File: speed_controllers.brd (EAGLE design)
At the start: 147.3 x 147.3 mm, 18 parts

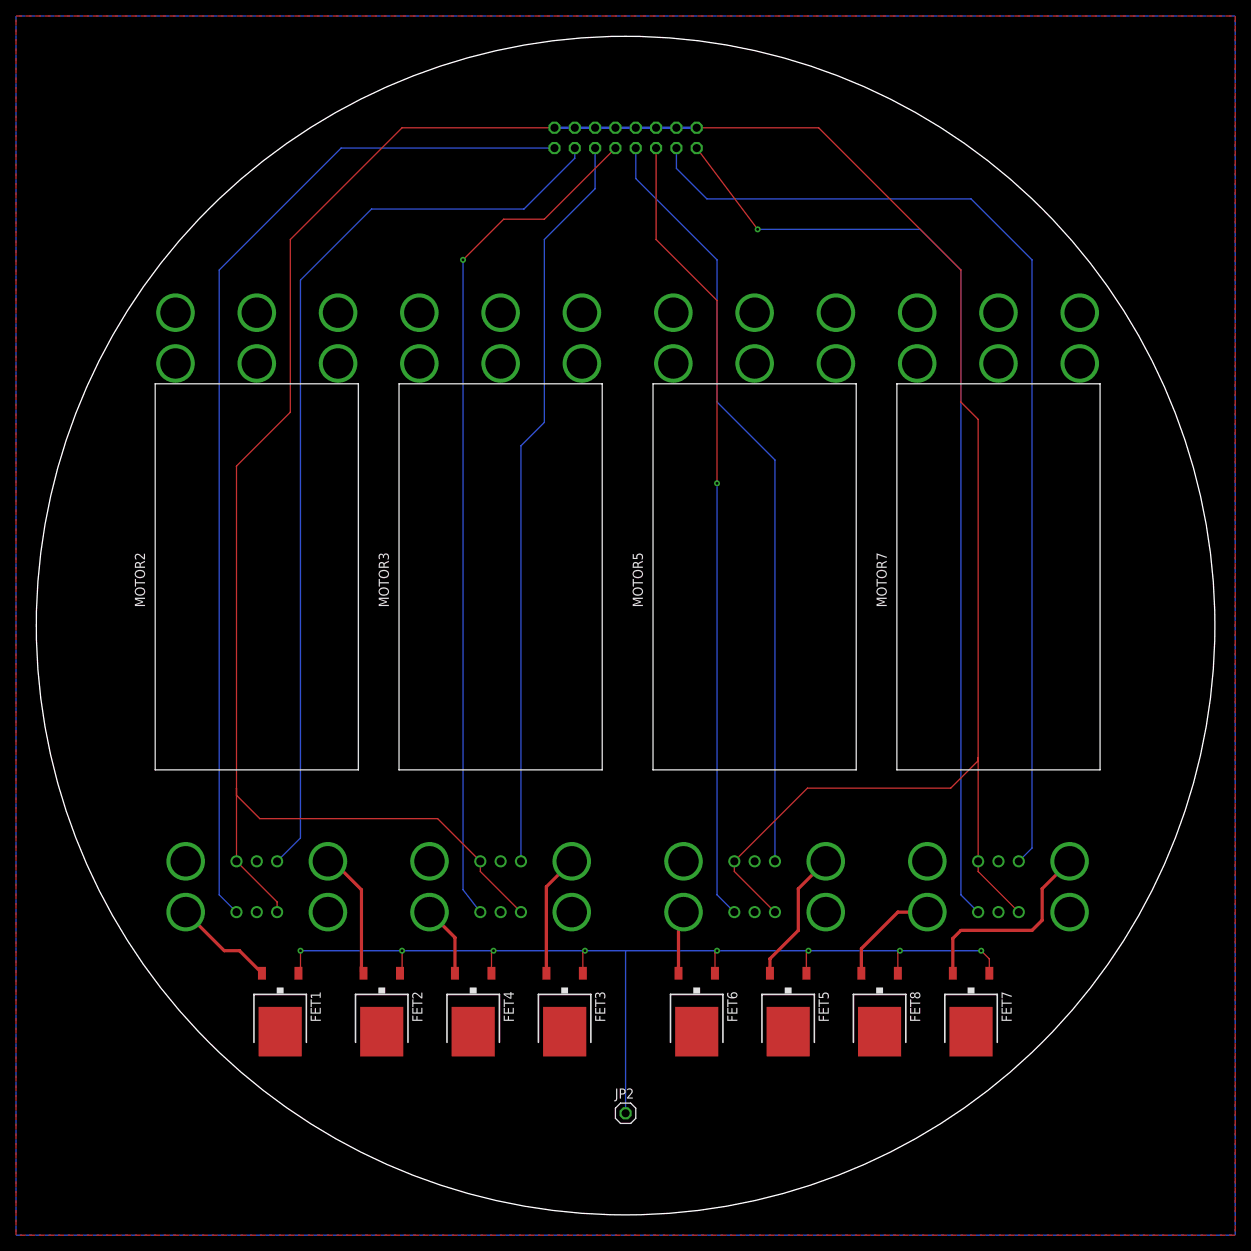
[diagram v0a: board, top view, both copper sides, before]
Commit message: Redone ESC boards
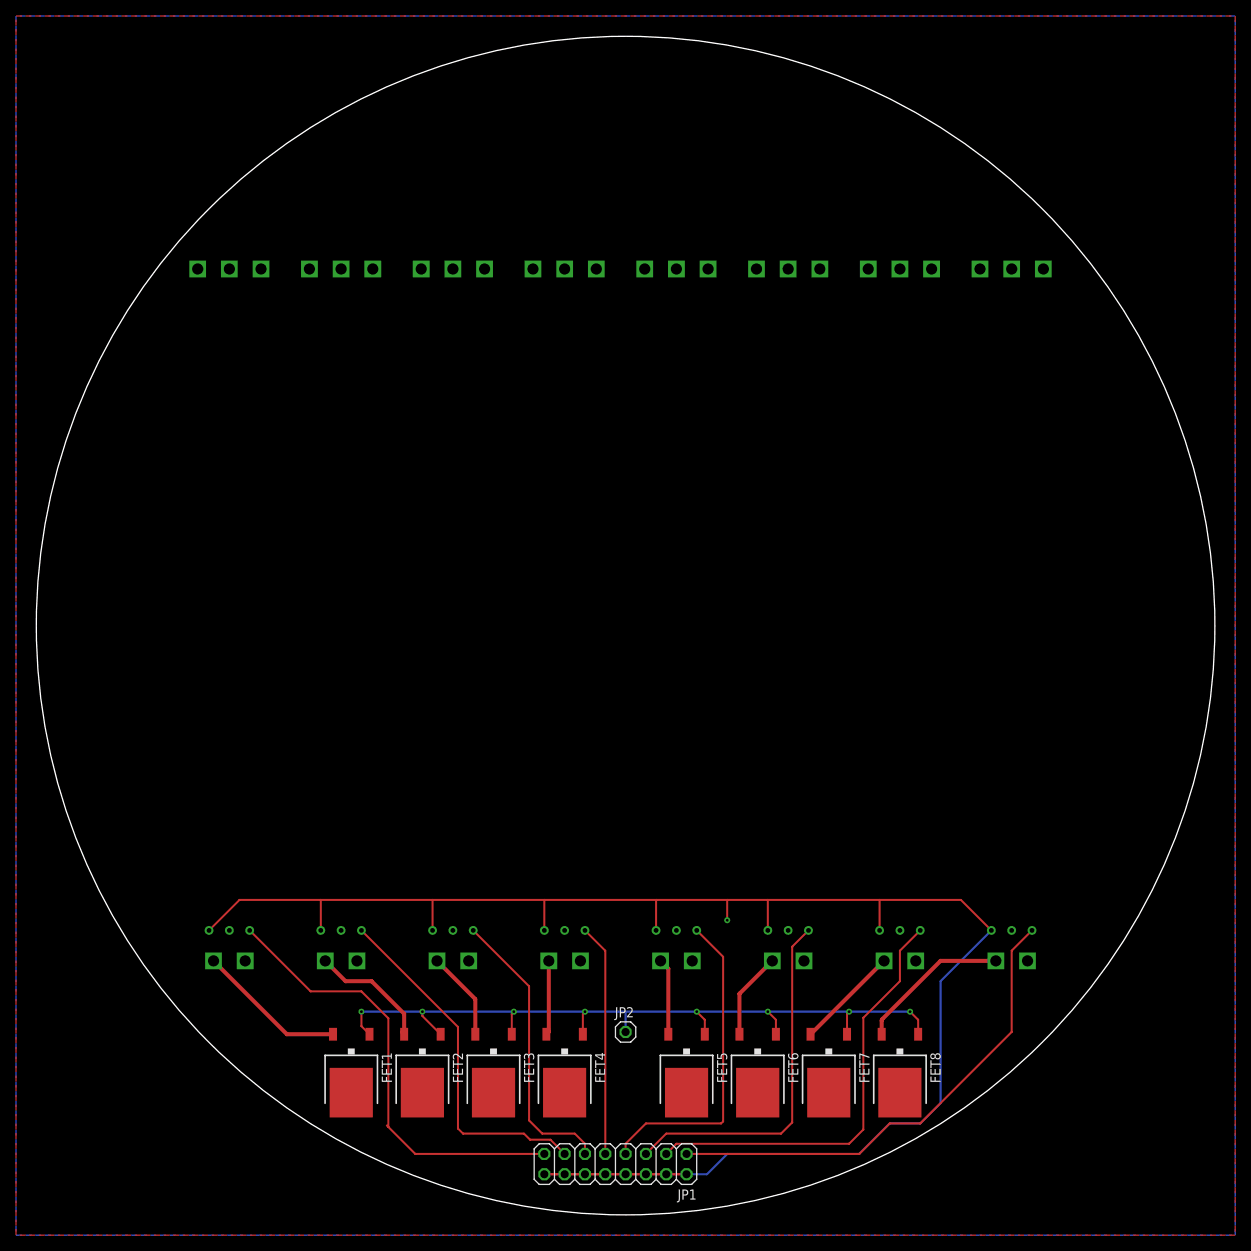
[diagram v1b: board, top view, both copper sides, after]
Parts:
- moved JP1 128.3 mm to (-1.27, -67.3), flipped to the top, turned to 180 degrees
- moved FET7 19.3 mm to (25.4, -55.9)
- moved FET5 14.8 mm to (7.62, -55.9)
- moved MOTOR7 13.7 mm to (34.3, 1.27), flipped to the bottom
- moved FET4 13.7 mm to (-7.62, -55.9)
- moved MOTOR2 12.2 mm to (-35.6, 1.27), flipped to the bottom
- moved FET1 11.7 mm to (-34.3, -55.9)
- moved FET3 11.7 mm to (-16.5, -55.9)
- moved MOTOR5 11.5 mm to (6.35, 1.27), flipped to the bottom
- moved FET6 10.8 mm to (16.5, -55.9)
- moved JP2 10.2 mm to (0.00, -50.8)
- moved FET2 9.16 mm to (-25.4, -55.9)
- moved MOTOR3 8.53 mm to (-21.6, 1.27), flipped to the bottom
- moved FET8 8.03 mm to (34.3, -55.9)
- moved MOTOR4 8.01 mm to (-7.62, 1.27)
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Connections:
- net VCC: no longer FET8.D
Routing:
- net N$2: track 357.0 -> 203.8 mm, vias 0 -> 1
- net N$6: track 107.1 -> 29.0 mm, vias 1 -> 0
- net N$12: track 127.6 -> 53.7 mm
- net N$14: track 129.4 -> 56.6 mm
- net N$11: track 115.7 -> 44.4 mm
- net N$13: track 121.4 -> 60.7 mm, vias 1 -> 0
- net N$10: track 93.0 -> 36.1 mm
- net N$4: track 96.4 -> 39.9 mm
- net N$1: track 99.6 -> 44.8 mm, vias 1 -> 0
- net N$20: track 129.1 -> 96.6 mm
- net N$8: track 25.3 -> 13.0 mm
- net N$5: track 16.9 -> 9.57 mm
- net N$3: track 12.7 -> 18.7 mm
- net N$18: track 13.2 -> 19.1 mm
- net N$16: track 15.3 -> 11.1 mm
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
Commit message: Fixed everything in issue Redone ESC boards #2
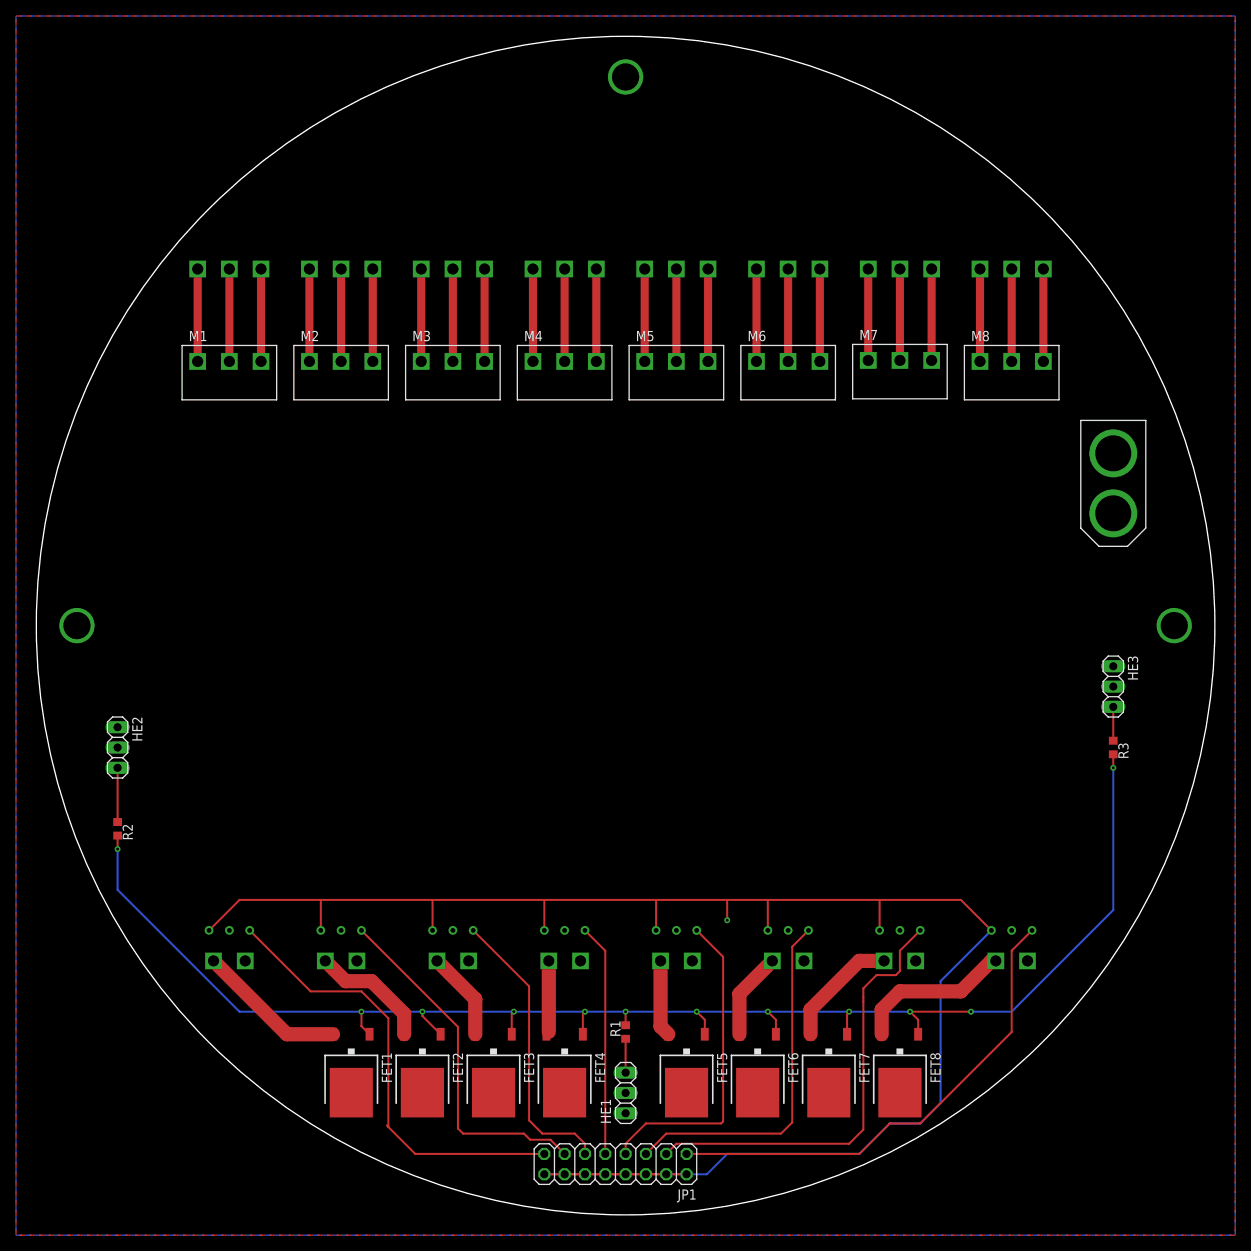
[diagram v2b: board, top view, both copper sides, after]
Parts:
- removed JP2: (no value), auv:1X01
- added HE1, HE2, HE3: (no value), auv:1X03
- added M1, M2, M3, M4, M5, M6, M7, M8: TE-1-1123723-3, auv:TE-1-1123723-3
- added R1, R2, R3: (no value), auv:R0603
- added U$1: XT-60, auv:XT-60
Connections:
- net N$1 renamed SIG_6
- net N$10 renamed SIG_3
- net N$11 renamed SIG_2
- net N$12 renamed SIG_7
- net N$13 renamed SIG_8
- net N$14 renamed SIG_1
- net N$15 renamed VIN_2
- net N$16 renamed VIN3
- net N$17 renamed VIN_4
- net N$18 renamed VIN_8
- net N$2 renamed PWM_GND
- net N$3 renamed VIN_1
- net N$4 renamed SIG_5
- net N$5 renamed VIN_5
- net N$6 renamed SIG_4
- net N$8 renamed VIN_7
- net N$9 renamed VIN_6
- removed net N$20: FET1.G, FET2.G, FET3.G, FET4.G, FET5.G, FET6.G, FET7.G, FET8.G, JP2.1
- new net FET_G: FET1.G, FET2.G, FET3.G, FET4.G, FET5.G, FET6.G, FET7.G, FET8.G, R1.2, R2.2, R3.2
- new net M1_1: M1.1, MOTOR1.MOTOR3
- new net M1_2: M1.2, MOTOR1.MOTOR2
- new net M1_3: M1.3, MOTOR1.MOTOR1
- new net M2_1: M2.1, MOTOR2.MOTOR3
- new net M2_2: M2.2, MOTOR2.MOTOR2
- new net M2_3: M2.3, MOTOR2.MOTOR1
- new net M3_1: M3.1, MOTOR3.MOTOR3
- new net M3_2: M3.2, MOTOR3.MOTOR2
- new net M3_3: M3.3, MOTOR3.MOTOR1
- new net M4_1: M4.1, MOTOR4.MOTOR3
- new net M4_2: M4.2, MOTOR4.MOTOR2
- new net M4_3: M4.3, MOTOR4.MOTOR1
- new net M5_1: M5.1, MOTOR5.MOTOR3
- new net M5_2: M5.2, MOTOR5.MOTOR2
- new net M5_3: M5.3, MOTOR5.MOTOR1
- new net M6_1: M6.1, MOTOR6.MOTOR3
- new net M6_2: M6.2, MOTOR6.MOTOR2
- new net M6_3: M6.3, MOTOR6.MOTOR1
- new net M7_1: M7.1, MOTOR7.MOTOR3
- new net M7_2: M7.2, MOTOR7.MOTOR2
- new net M7_3: M7.3, MOTOR7.MOTOR1
- new net M8_1: M8.1, MOTOR8.MOTOR3
- new net M8_2: M8.2, MOTOR8.MOTOR2
- new net M8_3: M8.3, MOTOR8.MOTOR1
- new net N$4: HE1.3, R1.1
- new net N$5: HE2.3, R2.1
- new net N$6: HE3.3, R3.1
- net GND: now also HE1.2, HE2.2, HE3.2, U$1.P$2
- net VCC: now also FET8.D, HE1.1, HE2.1, HE3.1, U$1.P$1
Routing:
- net FET_G: track 0.00 -> 189.5 mm, vias 0 -> 12
- net N$20: track 96.6 -> 0.00 mm, vias 8 -> 0
- net M8_3: track 0.00 -> 11.6 mm
- net M8_2: track 0.00 -> 11.6 mm
- net M8_1: track 0.00 -> 11.6 mm
- net M6_3: track 0.00 -> 11.6 mm
- net M6_2: track 0.00 -> 11.6 mm
- net M6_1: track 0.00 -> 11.6 mm
- net M5_3: track 0.00 -> 11.6 mm
- net M5_2: track 0.00 -> 11.6 mm
- net M5_1: track 0.00 -> 11.6 mm
- net M4_3: track 0.00 -> 11.6 mm
- net M4_2: track 0.00 -> 11.6 mm
- net M4_1: track 0.00 -> 11.6 mm
- net M3_3: track 0.00 -> 11.6 mm
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
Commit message: Added Optocoupler and Hall effect sensors
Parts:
- removed R2, R3: (no value), auv:R0603
- added OK1: 6N137, auv:DIL08
- JP1: device auv:2X08 -> auv:2X10
- moved HE2 26.0 mm to (-62.9, 10.8)
- moved R1 5.08 mm to (0.00, -45.7)
- moved HE1 2.54 mm to (0.00, -55.9)
- moved JP1 0.57 mm to (-1.02, -67.8)
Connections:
- removed net N$6: HE3.3, R3.1
- net FET_G: now also HE1.3, HE2.3, HE3.3, R1.1; no longer R1.2, R2.2, R3.2
- net GND: now also OK1.3
- net N$4: now also JP1.1, OK1.7, OK1.8; no longer HE1.3, R1.1
- net N$5: now also JP1.3, OK1.6; no longer HE2.3, R2.1
- net PWM_GND: now also JP1.18, JP1.20, OK1.5
- net SIG_1: now also JP1.19; no longer JP1.15
- net SIG_2: now also JP1.17; no longer JP1.13
- net SIG_3: now also JP1.15; no longer JP1.11
- net SIG_4: now also JP1.13; no longer JP1.9
- net SIG_5: now also JP1.11; no longer JP1.7
- net SIG_6: now also JP1.9; no longer JP1.5
- net SIG_7: now also JP1.7; no longer JP1.3
- net SIG_8: now also JP1.5; no longer JP1.1
- net VCC: now also OK1.2, R1.2
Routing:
- net N$4: track 4.23 -> 116.5 mm, vias 0 -> 1
- net N$5: track 6.77 -> 108.4 mm, vias 0 -> 1
- net PWM_GND: track 203.8 -> 258.0 mm, vias 1 -> 2
- net FET_G: track 189.5 -> 236.5 mm, vias 12 -> 11
- net N$6: track 4.23 -> 0.00 mm
- net SIG_5: track 39.9 -> 43.5 mm
- net SIG_3: track 36.1 -> 33.3 mm
- net SIG_6: track 44.8 -> 47.3 mm
- net SIG_7: track 55.2 -> 57.6 mm
- net SIG_8: track 60.7 -> 63.2 mm
- net SIG_1: track 56.6 -> 54.3 mm
- net SIG_2: track 44.4 -> 42.5 mm
- net SIG_4: track 29.0 -> 30.7 mm

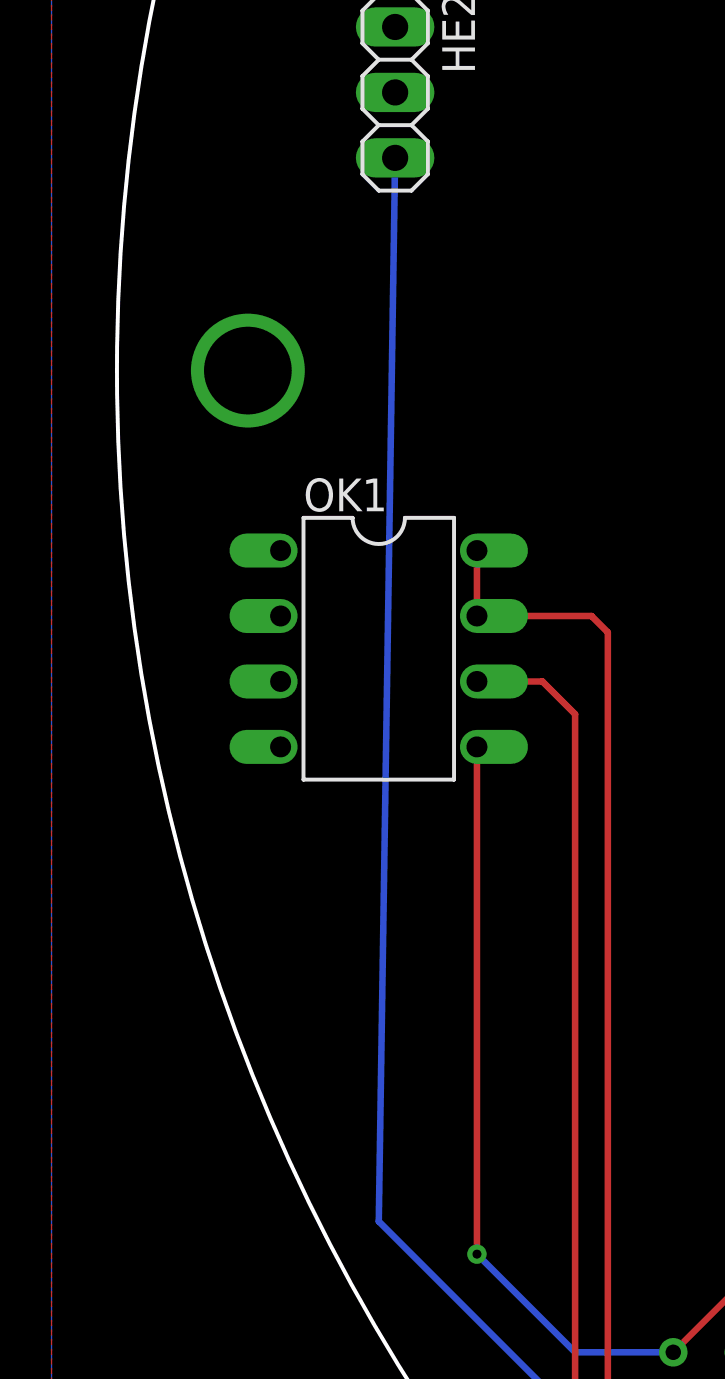
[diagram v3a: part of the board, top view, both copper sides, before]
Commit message: Rewired optocontroller
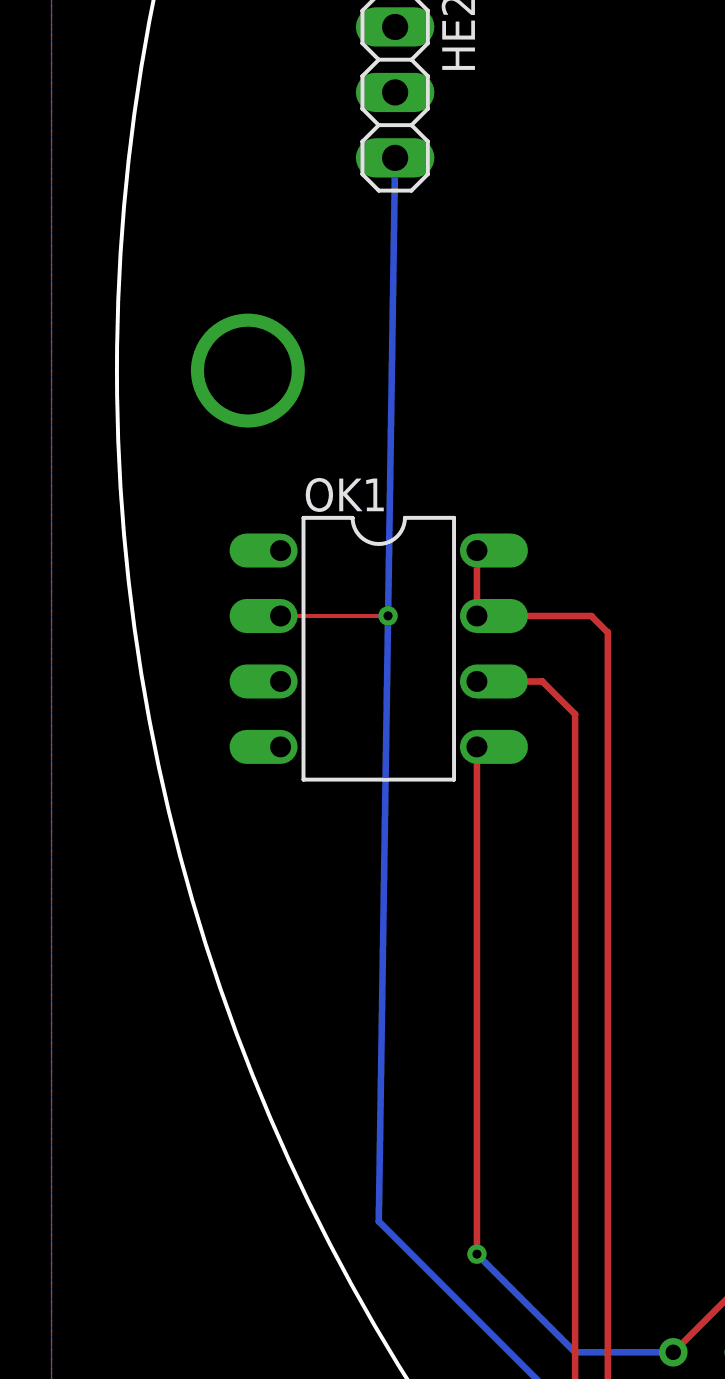
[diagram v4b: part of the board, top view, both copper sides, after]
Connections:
- net FET_G: now also OK1.2
- net VCC: no longer OK1.2
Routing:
- net FET_G: track 236.5 -> 240.6 mm, vias 11 -> 12
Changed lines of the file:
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@@
 <contactref element="HE3" pad="1"/>
 <contactref element="R1" pad="2"/>
-<contactref element="OK1" pad="2"/>
 </signal>
 <signal name="FET_G">
@@
 <wire x1="0" y1="-46.57" x2="0" y2="-48.26" width="0.1524" layer="1"/>
 <wire x1="0" y1="-48.26" x2="0" y2="-53.34" width="0.1524" layer="1"/>
-<wire x1="-62.865" y1="8.255" x2="-63.5" y2="-33.02" width="0.254" layer="16"/>
+<wire x1="-62.865" y1="8.255" x2="-63.138475" y2="-9.52079375" width="0.254" layer="16"/>
+<wire x1="-63.138475" y1="-9.52079375" x2="-63.5" y2="-33.02" width="0.254" layer="16"/>
 <wire x1="-63.5" y1="-33.02" x2="-48.26" y2="-48.26" width="0.254" layer="16"/>
 <wire x1="-48.26" y1="-48.26" x2="-33.02" y2="-48.26" width="0.254" layer="16"/>
@@
 <wire x1="50.8" y1="-48.26" x2="60.96" y2="-38.1" width="0.254" layer="1"/>
 <wire x1="60.96" y1="-38.1" x2="60.96" y2="-10.16" width="0.254" layer="1"/>
+<contactref element="OK1" pad="2"/>
+<wire x1="-67.31" y1="-9.525" x2="-63.14268125" y2="-9.525" width="0.1524" layer="1"/>
+<wire x1="-63.14268125" y1="-9.525" x2="-63.138475" y2="-9.52079375" width="0.1524" layer="1"/>
+<via x="-63.138475" y="-9.52079375" extent="1-16" drill="0.35"/>
 </signal>
 <signal name="PWM_GND">
